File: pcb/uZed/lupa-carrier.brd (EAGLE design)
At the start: 100 x 80 mm, 20 parts

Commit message: more work on carrier test
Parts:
- added C10, C8, C9: .1uF, rcl:C0603
- added JP1: (no value), pinhead:1X02
- added K1: 694108105102, Wurth_Elektronik_Electromechanic_DC_Power_Jack_Connectors_rev15c:694108105102
- added R10: 120, rcl:R0603
- added R11, R13, R14, R8: 1k, rcl:R0603
- added R12: 1k5, rcl:R0603
- added R15: 3k74, rcl:R0603
- added R16: 0, rcl:R0603
- added R17: 3k, rcl:R0603
- added R18: 100k, rcl:R0603
- added R5: 45k3, rcl:R0603
- added R6: 10k, rcl:R0603
- added R7: 3k92, rcl:R0603
- added R9: 220, rcl:R0603
- added U$10: AP331A, lupa300-components:SOT25
- added U$8: BAT54L, lupa300-components:SOT23
- added U$9: TL431A, lupa300-components:SOT23
- U$7: value BERGSTAK-100POS -> BSS138; device lupa300-components:BERG100POS -> lupa300-components:SOT23
- moved R4 119.9 mm to (43.8, 12.7)
- moved U$1 117.5 mm to (87.0, 1.27), flipped to the bottom, turned to 90 degrees
- moved C4 113.6 mm to (56.5, 13.3), turned to 180 degrees
- moved C7 112.1 mm to (52.1, 29.2), turned to 270 degrees
- moved C5 111.3 mm to (60.3, 45.7), turned to 180 degrees
- moved C6 107.4 mm to (52.1, 45.1), turned to 180 degrees
- moved C2 104.4 mm to (51.4, 12.1), turned to 270 degrees
- moved C1 102.8 mm to (55.2, 23.5), turned to 270 degrees
- moved R3 102.8 mm to (32.4, 17.8)
- moved JX1 99.9 mm to (70.5, 3.17)
- moved JX2 99.7 mm to (70.5, 47.6)
- moved U$6 97.3 mm to (56.5, 16.5), turned to 180 degrees
- moved U$5 96.5 mm to (59.7, 15.9)
- moved C3 94.6 mm to (39.4, 19.7), turned to 270 degrees
- moved U$4 88.0 mm to (61.0, 23.5)
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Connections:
- net PGOOD_CARRIER renamed PG_CARRIER
- removed net 3V3: JX1.P$21, JX1.P$23, JX2.P$21, JX2.P$23
- removed net HDMI_CLOCK: JX1.P$60
- new net 2V5_REF: C8.1, R11.2, R12.1, U$9.1, U$9.2
- new net N$8: R9.1, U$8.1
- new net N$9: C10.2, R16.1, R17.1, U$10.4
- net 5V: now also JX2.P$89, R17.2, R8.2, R9.2
- net 5V_OFF: now also R7.2, U$7.1
- net GND: now also C8.2, C9.2, JX1.P$24, JX2.P$24, K1.2, K1.3, R10.2, R13.1, R15.2, R18.1, R6.1, R7.1, U$10.2, U$7.2, U$9.3
- net N$2: now also R5.1, R6.2, U$4.3; no longer U$7.P$96
- net N$5: now also R12.2, R13.2, U$10.3; no longer U$7.P$35, U$7.P$49, U$7.P$55, U$7.P$61, U$7.P$67, U$7.P$73, U$7.P$79, U$7.P$85
- net N$6: now also JP1.1, R8.1; no longer U$7.P$86
- net N$7: now also C10.1, R14.2, R15.1, U$10.1; no longer U$7.P$41, U$7.P$43
- net VADJ_EN: now also R16.2, R18.2
- net VCCIO: now also JX1.P$21, JX1.P$22, JX1.P$23, JX2.P$21, JX2.P$22, JX2.P$23, R5.2
- net VCCIO_EN: now also JP1.2, R10.1, R14.1, U$7.3, U$8.3
- net VIN: now also C9.1, K1.1, R11.1, U$10.5
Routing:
- net 5V: track 0.00 -> 216.0 mm
- net GND: track 0.00 -> 133.6 mm, vias 0 -> 11
- net VCCIO: track 0.00 -> 77.5 mm, vias 0 -> 2
- net VIN: track 0.00 -> 67.3 mm, vias 0 -> 1
- net 5V_OFF: track 0.00 -> 62.6 mm, vias 0 -> 1
- net VCCIO_EN: track 0.00 -> 41.5 mm
- net N$7: track 0.00 -> 17.2 mm, vias 0 -> 2
- net 2V5_REF: track 0.00 -> 15.1 mm
- net PWR_EN: track 0.00 -> 15.1 mm
- net N$9: track 0.00 -> 13.1 mm
- net N$1: track 0.00 -> 9.82 mm
- net N$2: track 0.00 -> 8.86 mm
- net N$4: track 0.00 -> 7.71 mm
- net N$3: track 0.00 -> 7.45 mm
- net VADJ_EN: track 0.00 -> 7.38 mm
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- added copper zone on layer 1, net GND
- added copper zone on layer 16, net GND
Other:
- board size 100 x 80 mm -> 101.3 x 57.1 mm

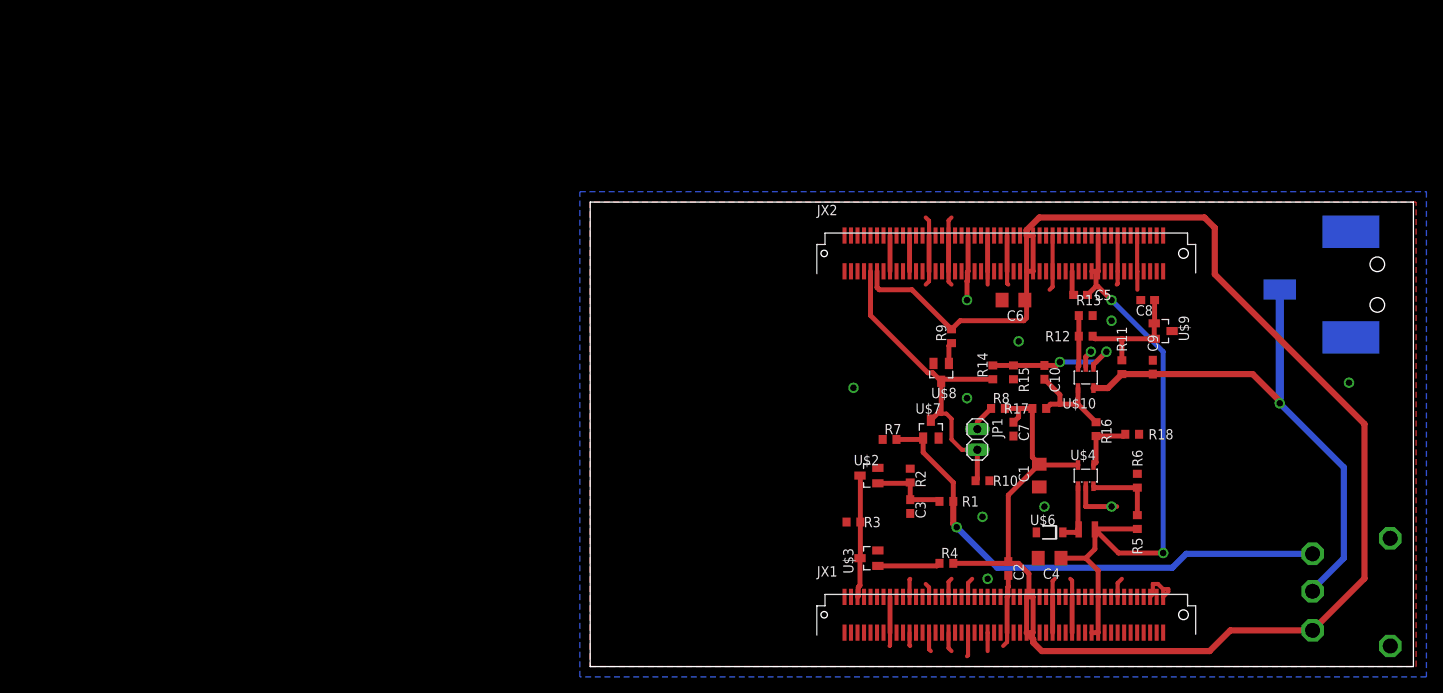
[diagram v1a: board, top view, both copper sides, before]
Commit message: tweaked layout, ready to fab
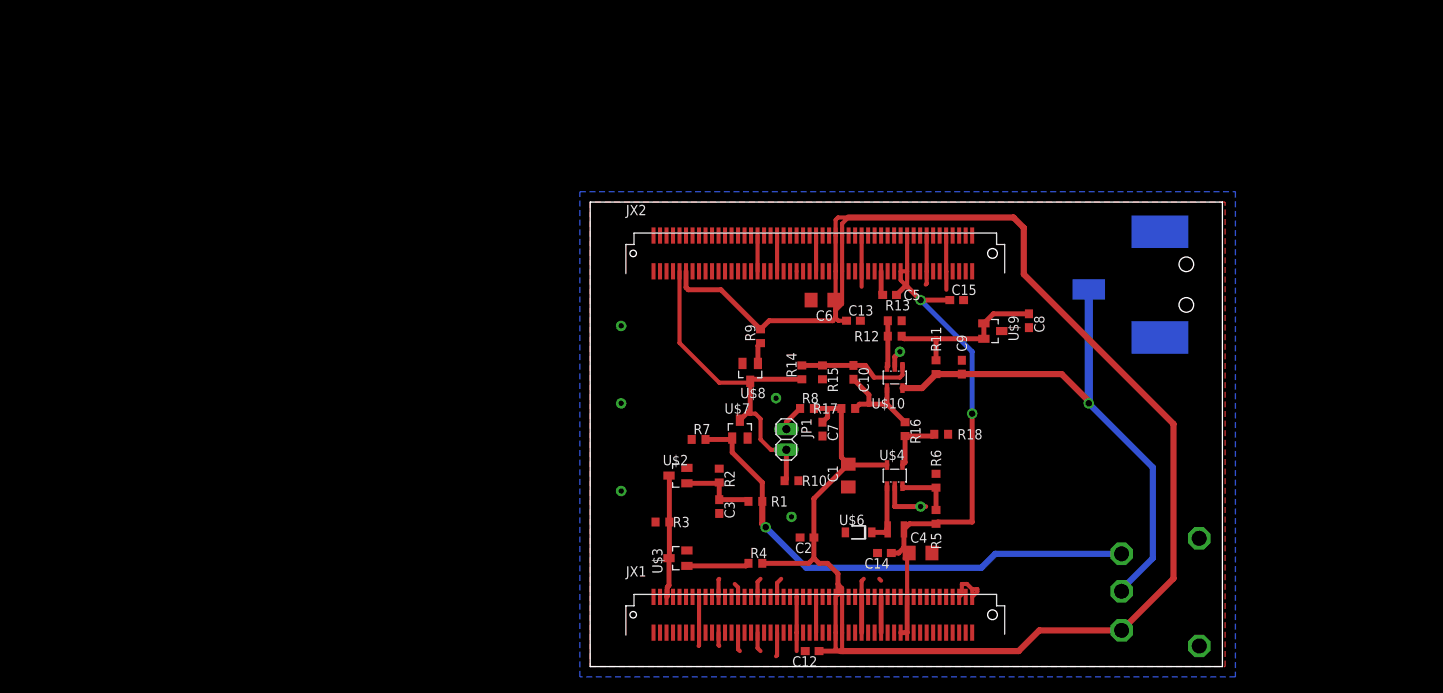
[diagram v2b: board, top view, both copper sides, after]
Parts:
- added C12, C13, C14, C15: .1uF, rcl:C0603
- moved C2 25.1 mm to (26.7, 15.9), turned to 180 degrees
- moved R5 24.8 mm to (42.5, 18.4)
- moved R6 24.8 mm to (42.5, 22.9)
- moved R13 23.5 mm to (37.5, 42.5)
- moved C10 23.5 mm to (32.4, 36.2)
- moved C5 23.5 mm to (36.8, 45.7)
- moved C9 23.5 mm to (45.7, 36.8)
- moved K1 23.5 mm to (76.8, 47.0)
- moved R9 23.5 mm to (21.0, 40.6)
- moved U$1 23.5 mm to (63.5, 1.27)
- moved C6 23.5 mm to (28.6, 45.1)
- moved C7 23.5 mm to (28.6, 29.2)
- moved JP1 23.5 mm to (24.1, 27.9)
- moved R14 23.5 mm to (26.0, 36.2)
- moved R15 23.5 mm to (28.6, 36.2)
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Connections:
- net 5V: now also C12.1, C13.1
- net GND: now also C12.2, C13.2, C14.2, C15.2
- net VCCIO: now also C14.1, C15.1
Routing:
- net GND: track 133.6 -> 95.6 mm, vias 11 -> 6
- net 5V: track 216.0 -> 230.4 mm
- net 2V5_REF: track 15.1 -> 20.8 mm
- net VCCIO: track 77.5 -> 72.2 mm
- net N$7: track 17.2 -> 14.5 mm, vias 2 -> 0
- net VCCIO_EN: track 41.5 -> 43.6 mm
- net N$2: track 8.86 -> 6.95 mm
- net N$5: track 6.36 -> 5.73 mm
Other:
- board size 101.3 x 57.1 mm -> 77.8 x 57.1 mm

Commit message: added 2A 3.3v reg to power suply design. made power supply layout more compact. increased board size
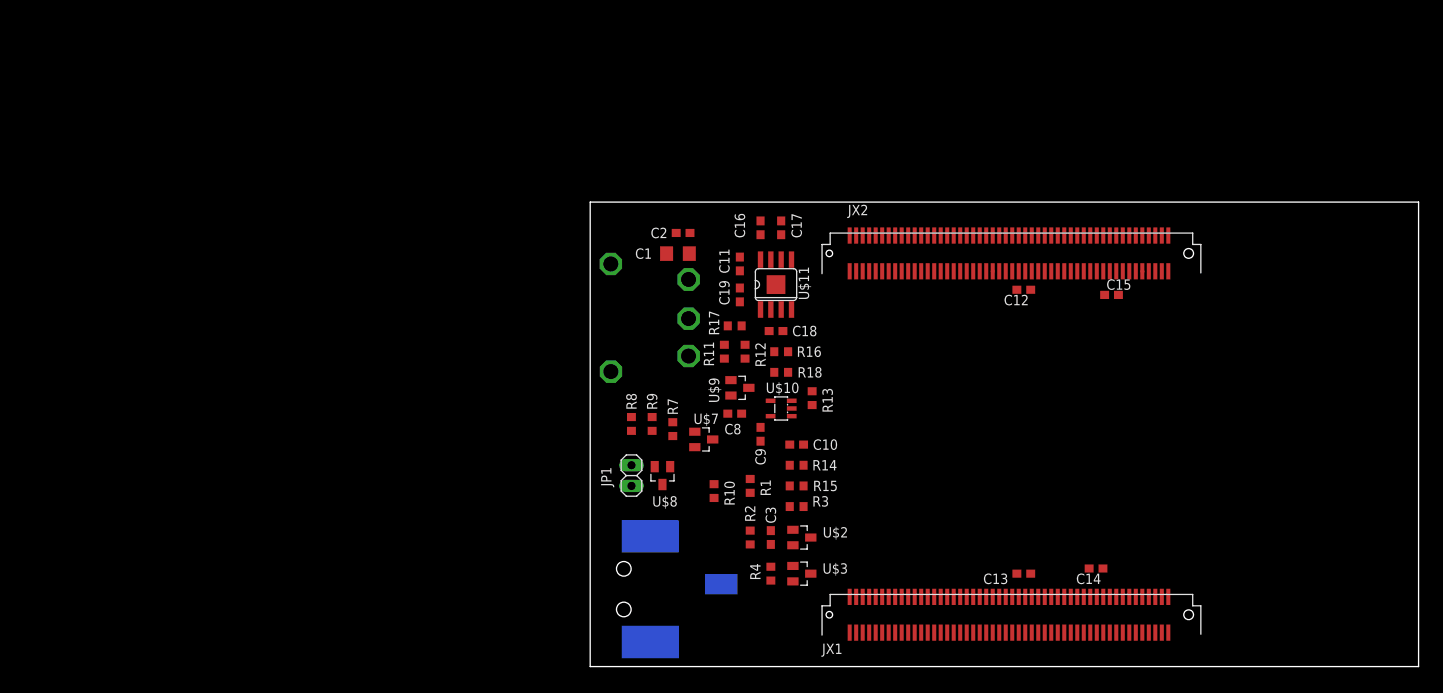
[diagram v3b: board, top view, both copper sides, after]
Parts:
- removed C4, C6: 22uF, rcl:C1206
- removed C5, C7: .1uF, rcl:C0603
- removed R5: 45k3, rcl:R0603
- removed R6: 10k, rcl:R0603
- removed U$4: LMR10510, lupa300-components:SOT25
- removed U$5: DFE252012R, lupa300-components:L2520
- removed U$6: MBR230LSFT1GFL, lupa300-components:SOD123FL
- added C11, C19: 10uF, rcl:C0603
- added C16, C17, C18: 1uF, rcl:C0603
- added U$11: ADP7158, lupa300-components:SO08
- moved K1 84.9 mm to (0.64, 9.53), turned to 180 degrees
- moved U$1 70.0 mm to (14.0, 50.8), turned to 270 degrees
- moved C12 51.5 mm to (53.3, 46.4)
- moved C2 40.4 mm to (11.4, 53.3)
- moved C8 38.0 mm to (17.8, 31.1), turned to 0 degrees
- moved C13 37.5 mm to (53.3, 11.4), turned to 180 degrees
- moved C1 34.4 mm to (10.8, 50.8), turned to 180 degrees
- moved U$9 31.9 mm to (18.4, 34.3)
- moved C9 26.1 mm to (21.0, 28.6), turned to 270 degrees
- moved R11 26.1 mm to (16.5, 38.7), turned to 270 degrees
- moved C14 26.1 mm to (62.2, 12.1)
- moved JX1 24.1 mm to (71.1, 3.17)
- moved JX2 24.1 mm to (71.1, 47.6)
- moved R8 21.7 mm to (5.08, 29.8), turned to 90 degrees
- moved R18 21.1 mm to (23.5, 36.2)
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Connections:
- removed net N$2: R5.1, R6.2, U$4.3
- removed net N$3: U$4.1, U$5.P$1, U$6.C
- new net N$10: C16.1, U$11.7
- new net N$11: C17.1, U$11.5, U$11.6
- new net N$12: C18.1, U$11.3
- net 5V: now also C11.1, U$11.8; no longer C6.1, C7.1, U$4.5
- net GND: now also C11.2, C16.2, C17.2, C18.2, C19.2, U$11.9; no longer C4.2, C5.2, C6.2, C7.2, R6.1, U$4.2, U$6.A
- net VADJ_EN: now also U$11.4; no longer U$4.4
- net VCCIO: now also C19.1, U$11.1, U$11.2; no longer C4.1, C5.1, R5.2, U$5.P$2
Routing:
- net 5V: track 230.4 -> 0.00 mm
- net GND: track 95.6 -> 0.05 mm, vias 6 -> 0
- net VCCIO: track 72.2 -> 0.00 mm, vias 2 -> 0
- net VIN: track 67.3 -> 0.00 mm, vias 1 -> 0
- net 5V_OFF: track 62.6 -> 0.00 mm, vias 1 -> 0
- net VCCIO_EN: track 43.6 -> 0.00 mm
- net 2V5_REF: track 20.8 -> 0.00 mm
- net PWR_EN: track 15.1 -> 0.00 mm
- net N$7: track 14.5 -> 0.00 mm
- net N$9: track 13.1 -> 0.00 mm
- net N$1: track 9.82 -> 0.00 mm
- net N$4: track 7.71 -> 0.00 mm
- net N$3: track 7.45 -> 0.00 mm
- net VADJ_EN: track 7.38 -> 0.00 mm
- net N$2: track 6.95 -> 0.00 mm
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- removed copper zone on layer 1, net GND
- removed copper zone on layer 16, net GND
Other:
- board size 77.8 x 57.1 mm -> 101.9 x 57.1 mm

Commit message: more lupa crrier layout work
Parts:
- moved JX1 44.5 mm to (71.1, 47.6)
- moved JX2 44.5 mm to (71.1, 3.17)
- moved R8 23.6 mm to (26.7, 20.3), turned to 0 degrees
- moved C3 21.0 mm to (5.08, 27.9), turned to 180 degrees
- moved U$2 20.7 mm to (6.35, 22.2), turned to 180 degrees
- moved R9 20.3 mm to (26.7, 22.9), turned to 0 degrees
- moved R2 17.8 mm to (5.08, 26.0), turned to 0 degrees
- moved R18 17.2 mm to (24.1, 53.3), turned to 270 degrees
- moved R3 15.9 mm to (9.53, 20.3), turned to 90 degrees
- moved U$3 15.9 mm to (13.3, 21.0), turned to 90 degrees
- moved JP1 15.7 mm to (20.3, 19.7), turned to 180 degrees
- moved U$8 13.3 mm to (22.2, 23.5), turned to 90 degrees
- moved R17 12.6 mm to (26.7, 33.0), turned to 0 degrees
- moved C18 12.5 mm to (26.0, 53.3), turned to 90 degrees
- moved R1 12.0 mm to (8.26, 26.0), turned to 0 degrees
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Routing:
- net 5V: track 0.00 -> 123.2 mm
- net VCCIO: track 0.00 -> 118.7 mm, vias 0 -> 8
- net VCCIO_EN: track 0.00 -> 50.0 mm, vias 0 -> 1
- net VADJ_EN: track 0.00 -> 30.4 mm, vias 0 -> 2
- net VIN: track 0.00 -> 14.0 mm
- net N$4: track 0.00 -> 13.3 mm
- net 5V_OFF: track 0.00 -> 12.7 mm
- net N$7: track 0.00 -> 10.3 mm
- net N$9: track 0.00 -> 9.78 mm
- net 2V5_REF: track 0.00 -> 9.09 mm
- net N$5: track 0.00 -> 7.78 mm
- net N$1: track 0.00 -> 6.13 mm
- net PWR_EN: track 0.00 -> 5.99 mm
- net N$10: track 0.00 -> 5.86 mm
- net N$12: track 0.00 -> 5.23 mm
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- added copper zone on layer 1, net GND
- added copper zone on layer 16, net GND

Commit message: almost done routing
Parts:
- moved R4 33.5 mm to (11.4, 47.6)
- moved R3 33.2 mm to (13.3, 53.3)
- moved U$3 29.9 mm to (11.4, 50.8), turned to 0 degrees
- moved U$2 9.71 mm to (8.26, 31.8), turned to 90 degrees
- moved C3 7.10 mm to (12.1, 29.2)
- moved R1 7.10 mm to (15.2, 27.3)
- moved R2 7.10 mm to (12.1, 27.3)
- moved R7 7.10 mm to (15.2, 29.2)
- moved C1 4.96 mm to (10.8, 45.7)
- moved U$7 4.02 mm to (15.9, 24.1), turned to 270 degrees
- moved C17 3.18 mm to (17.8, 52.7), turned to 0 degrees
- moved C2 2.62 mm to (9.53, 41.9), turned to 270 degrees
- moved R14 2.62 mm to (19.1, 27.3)
- moved C16 2.54 mm to (15.2, 50.8)
- moved R10 2.54 mm to (19.1, 24.1), turned to 270 degrees
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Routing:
- net PWR_EN: track 5.99 -> 49.0 mm
- net VIN: track 14.0 -> 50.1 mm, vias 0 -> 5
- net N$4: track 13.3 -> 2.12 mm
- net N$11: track 3.70 -> 10.2 mm
- net VCCIO: track 118.7 -> 125.1 mm
- net VCCIO_EN: track 50.0 -> 44.1 mm, vias 1 -> 0
- net N$10: track 5.86 -> 3.32 mm
- net N$5: track 7.78 -> 9.93 mm
- net N$1: track 6.13 -> 8.22 mm
- net N$7: track 10.3 -> 8.30 mm
- net N$6: track 4.49 -> 3.22 mm
- net 5V: track 123.2 -> 122.1 mm
- net N$12: track 5.23 -> 4.59 mm

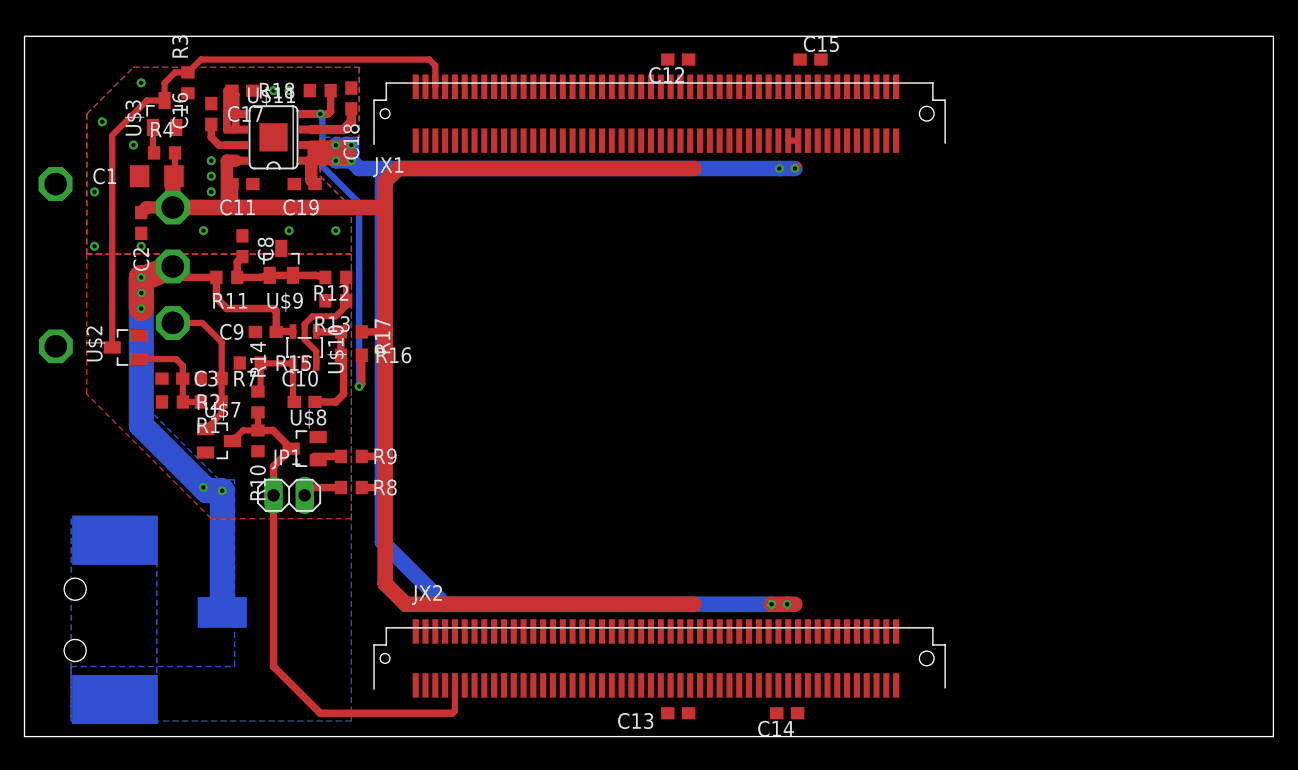
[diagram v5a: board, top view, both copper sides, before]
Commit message: finished improved power supply layout
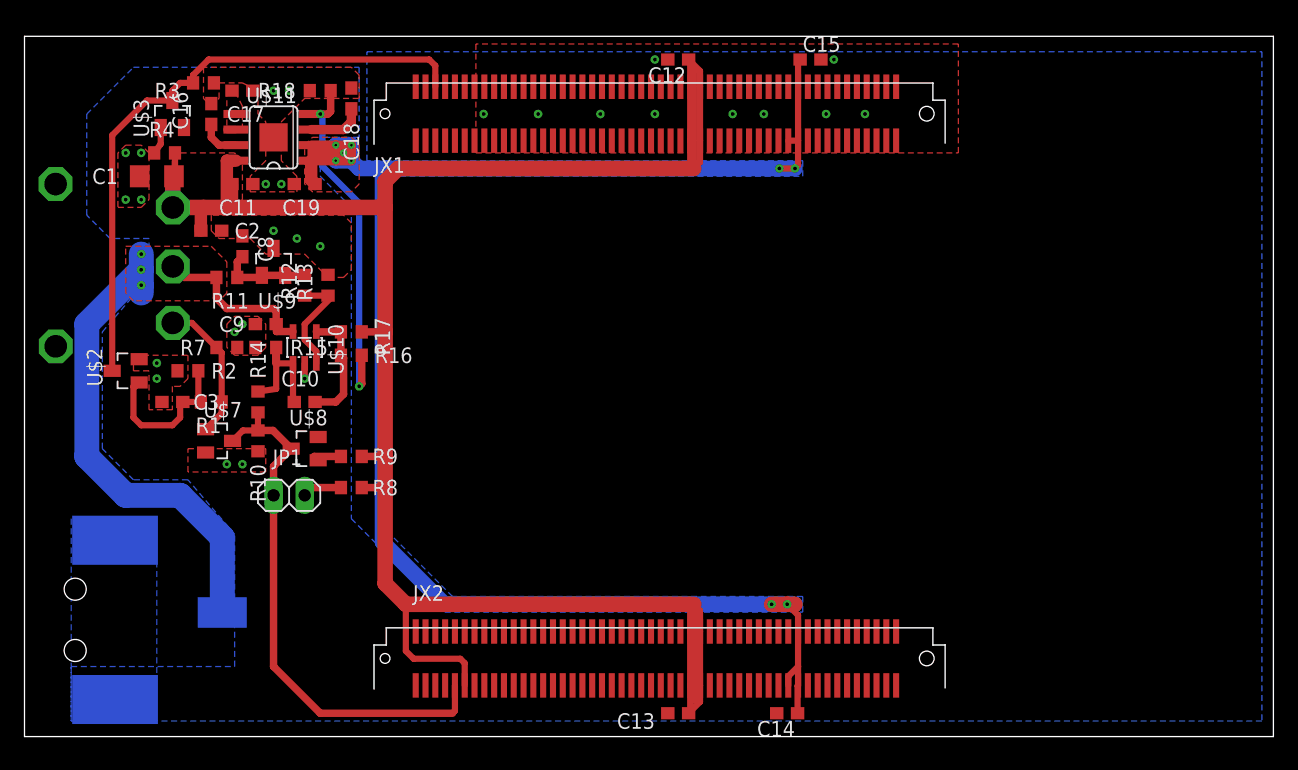
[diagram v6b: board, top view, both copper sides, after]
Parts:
- moved C2 5.75 mm to (15.2, 41.3), turned to 0 degrees
- moved R2 2.84 mm to (13.3, 29.8)
- moved R7 2.84 mm to (16.5, 31.8), turned to 180 degrees
- moved R12 2.62 mm to (22.9, 36.8), turned to 270 degrees
- moved C3 1.91 mm to (12.1, 27.3)
- moved U$2 1.91 mm to (8.26, 29.8)
- moved R15 1.80 mm to (19.7, 31.8)
- moved R13 1.42 mm to (24.8, 36.8), turned to 270 degrees
- moved R3 1.27 mm to (14.6, 53.3), turned to 180 degrees
- moved U$3 0.63 mm to (12.1, 50.8)
- moved C9 0.63 mm to (19.7, 33.7)
- moved U$9 0.63 mm to (20.3, 38.7)
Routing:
- net 5V: track 122.1 -> 169.1 mm
- net VCCIO: track 125.1 -> 148.2 mm, vias 8 -> 9
- net N$11: track 10.2 -> 0.74 mm
- net N$3: track 0.00 -> 7.62 mm
- net N$2: track 0.00 -> 6.99 mm
- net N$1: track 8.22 -> 12.9 mm
- net VIN: track 50.1 -> 54.1 mm, vias 5 -> 3
- net N$7: track 8.30 -> 12.1 mm
- net PWR_EN: track 49.0 -> 50.9 mm
- net 2V5_REF: track 9.09 -> 7.44 mm
- net GND: track 0.00 -> 1.24 mm, vias 14 -> 28
- net N$5: track 9.93 -> 8.80 mm
- added copper zone on layer 1, net 5V
- added copper zone on layer 1, net N$11
- added copper zone on layer 1, net VCCIO
- added copper zone on layer 1, net VIN
